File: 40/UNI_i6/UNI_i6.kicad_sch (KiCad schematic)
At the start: 144 parts, among them J1 ZX-SH1.0-4PWT, J3 Conn_01x05, SW1 MX_SW_solder, SW10 MX_SW_solder, SW11 MX_SW_solder, SW12 MX_SW_solder, SW13 MX_SW_solder, SW14 MX_SW_solder, SW15 MX_SW_solder, SW16 MX_SW_solder, SW17 MX_SW_solder, SW18 MX_SW_solder, SW19 MX_SW_solder, SW2 MX_SW_solder, SW20 MX_SW_solder, SW21 MX_SW_solder, SW22 MX_SW_solder, SW23 MX_SW_solder, SW24 MX_SW_solder, SW25 MX_SW_solder, SW26 MX_SW_solder, SW27 MX_SW_solder, SW28 MX_SW_solder, SW29 MX_SW_solder, SW3 MX_SW_solder, SW30 MX_SW_solder, SW31 MX_SW_solder, SW32 MX_SW_solder, SW33 MX_SW_solder, SW34 MX_SW_solder, SW35 MX_SW_solder, SW36 MX_SW_solder, SW37 MX_SW_solder, SW38 MX_SW_solder, SW39 MX_SW_solder, SW4 MX_SW_solder, SW40 MX_SW_solder, SW41 MX_SW_solder, SW42 MX_SW_solder, SW43 MX_SW_solder, SW44 MX_SW_solder, SW45 MX_SW_solder, SW46 MX_SW_solder, SW47 MX_SW_solder, SW48 MX_SW_solder, SW49 MX_SW_solder, SW5 MX_SW_solder, SW50 MX_SW_solder, SW6 MX_SW_solder, SW7 MX_SW_solder, SW78 SW_RESET, SW79 SW_BOOTSEL, SW8 MX_SW_solder, SW9 MX_SW_solder, U1 RP2040, U2 XC6206PxxxMR, U4 W25Q128JVS, Y1 Crystal_GND24

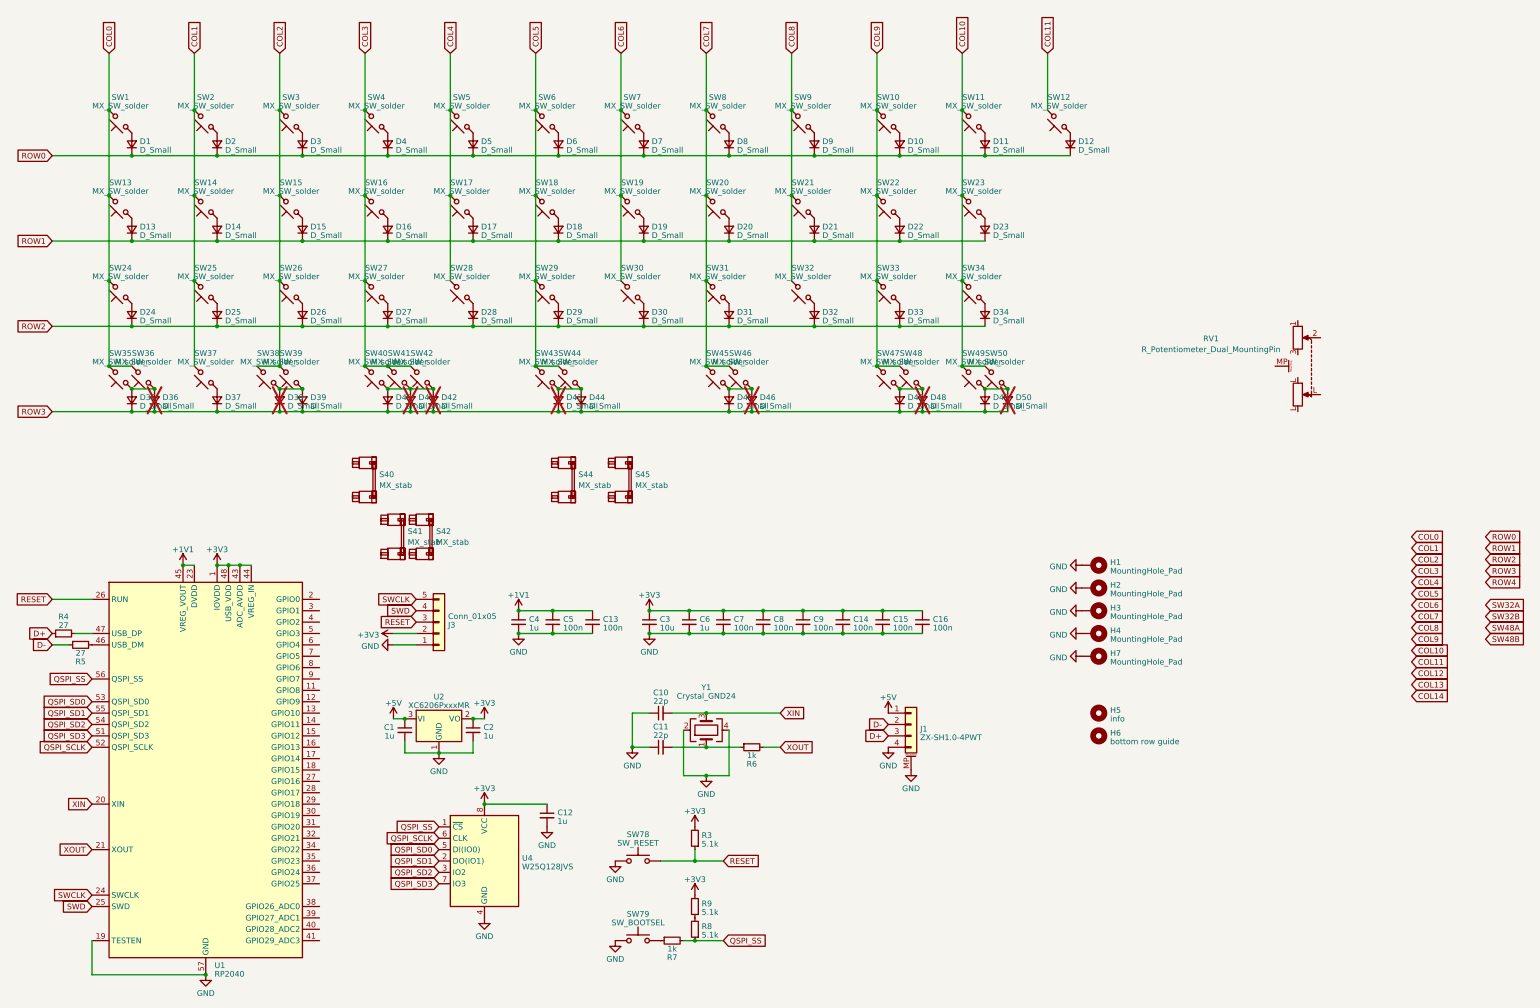
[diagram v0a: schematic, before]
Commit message: i5v6 ported to tako
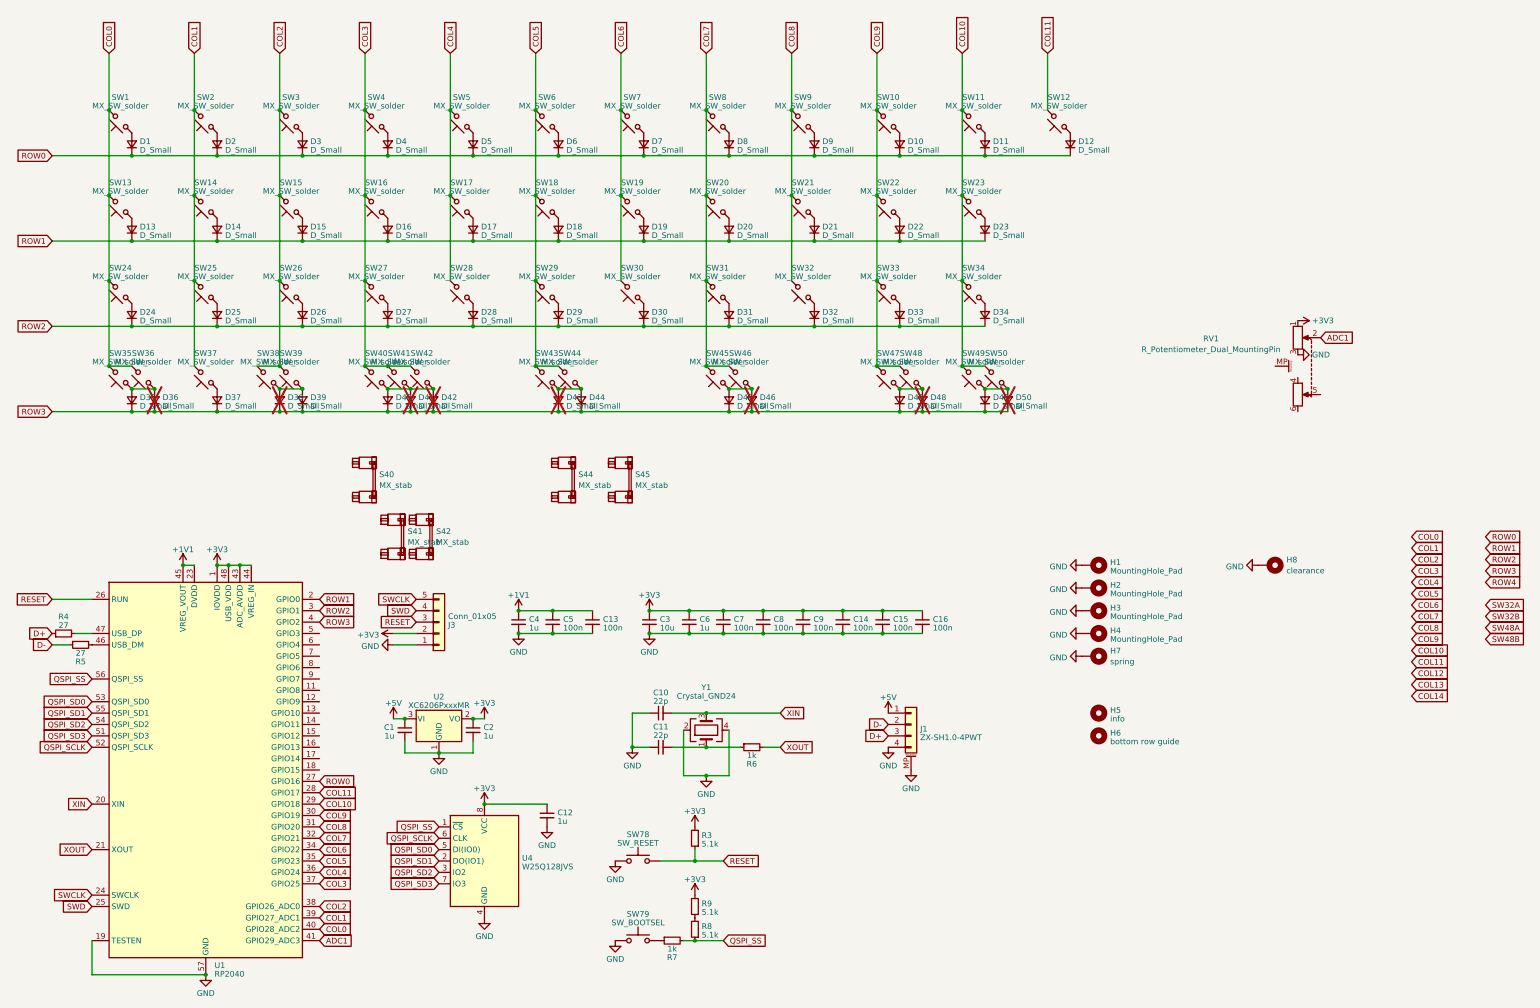
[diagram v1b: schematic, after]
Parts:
- added H8: clearance, MountingHole:MountingHole_2.2mm_M2_Pad, symbol Mechanical:MountingHole_Pad
- H7: value MountingHole_Pad -> spring; LCSC Part Number (none) -> C30167254
- RV1: footprint (none) -> shoonies_parts:RS6011YA600M
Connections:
- net +3V3: now also RV1.1
- net COL0: now also U1.40 (GPIO28_ADC2)
- net COL1: now also U1.39 (GPIO27_ADC1)
- net COL10: now also U1.29 (GPIO18)
- net COL11: now also U1.28 (GPIO17)
- net COL2: now also U1.38 (GPIO26_ADC0)
- net COL3: now also U1.37 (GPIO25)
- net COL4: now also U1.36 (GPIO24)
- net COL5: now also U1.35 (GPIO23)
- net COL6: now also U1.34 (GPIO22)
- net COL7: now also U1.32 (GPIO21)
- net COL8: now also U1.31 (GPIO20)
- net COL9: now also U1.30 (GPIO19)
- net GND: now also RV1.3, H8.1
- net ROW0: now also U1.27 (GPIO16)
- net ROW1: now also U1.2 (GPIO0)
- net ROW2: now also U1.3 (GPIO1)
- net ROW3: now also U1.4 (GPIO2)
- net ADC1: now reaches U1.41 (GPIO29_ADC3)
- net ADC1: now also RV1.2
